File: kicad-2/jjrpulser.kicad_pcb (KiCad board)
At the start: 2 copper layers, 33.8 x 48 mm, 24 parts, among them J1 Conn_Coaxial_Power, J3 Screw_Terminal_HOT, J4 Screw_Terminal_COLD, J5 Conn_UART, U1 ESP-12, U2 AMS1117-3.3_SOT223

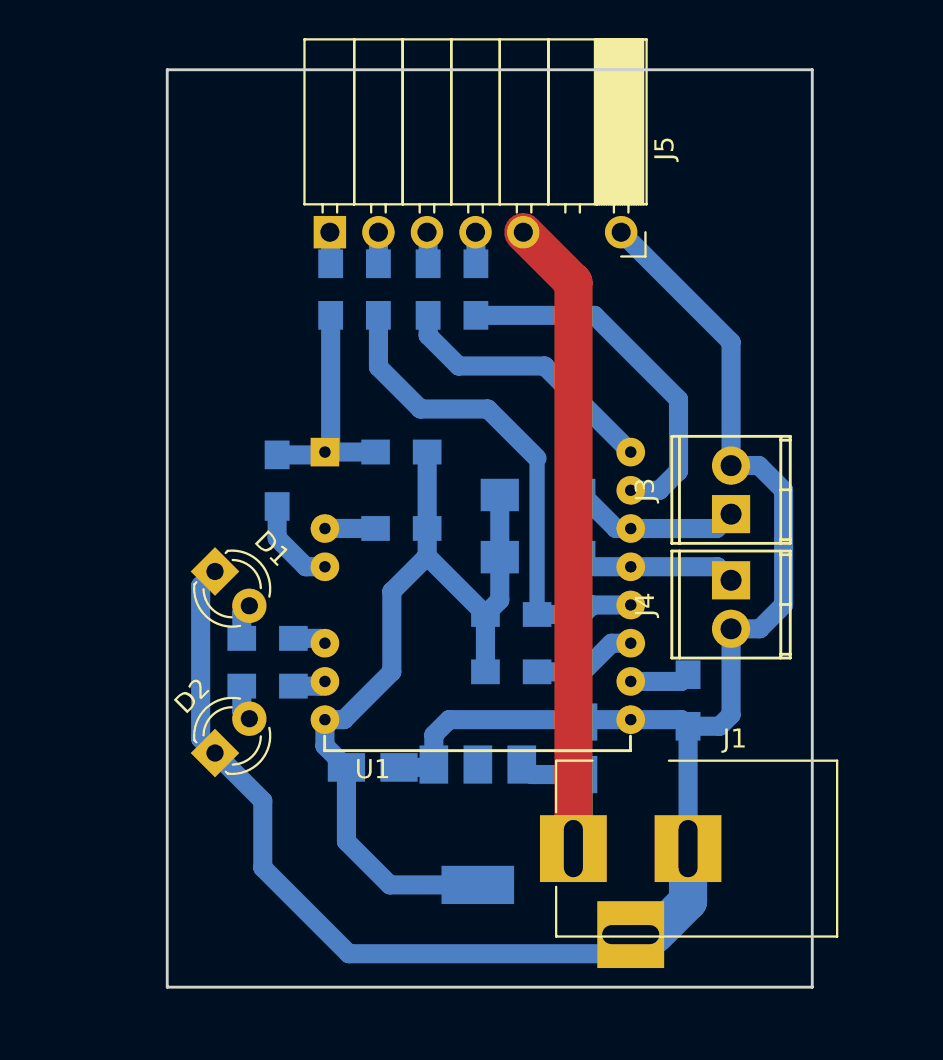
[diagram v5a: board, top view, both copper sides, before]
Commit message: Разводка2: Защитные резисторы на подключении водосчетчиков
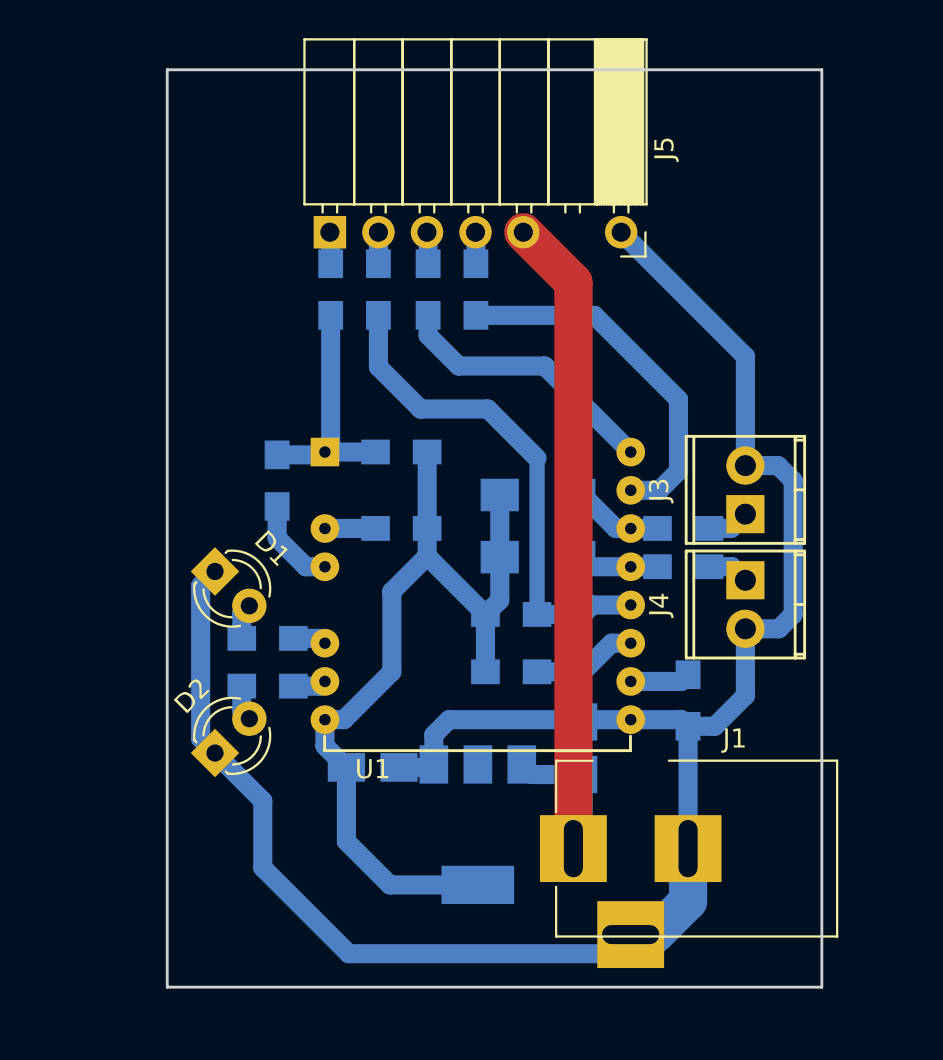
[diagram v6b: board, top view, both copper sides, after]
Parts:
- added R15: 470, Resistors_SMD:R_0805_HandSoldering, B.Cu at (166.2, 109.0)
- added R16: 470, Resistors_SMD:R_0805_HandSoldering, B.Cu at (166.2, 111.0)
- moved J3 0.75 mm to (169.5, 108.2)
- moved J4 0.75 mm to (169.5, 114.2)
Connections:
- R10 pad 2: Net-(J4-Pad1) -> Net-(R10-Pad2)
- R5 pad 1: Net-(J3-Pad2) -> Net-(R15-Pad2)
- U1 pad 13: Net-(J4-Pad1) -> Net-(R10-Pad2)
- U1 pad 14: Net-(J3-Pad2) -> Net-(R15-Pad2)
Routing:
- net Net-(J3-Pad2): track 9.14 -> 2.21 mm
- net Net-(J4-Pad1): track 8.60 -> 2.19 mm
- net Net-(R15-Pad2): track 0.00 -> 4.98 mm
- net Net-(R10-Pad2): track 0.00 -> 4.46 mm
- net Earth: track 101.2 -> 101.7 mm
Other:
- board size 33.8 x 48 mm -> 34.2 x 48 mm

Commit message: Новые маленькие коннекторы для счетчиков и питания
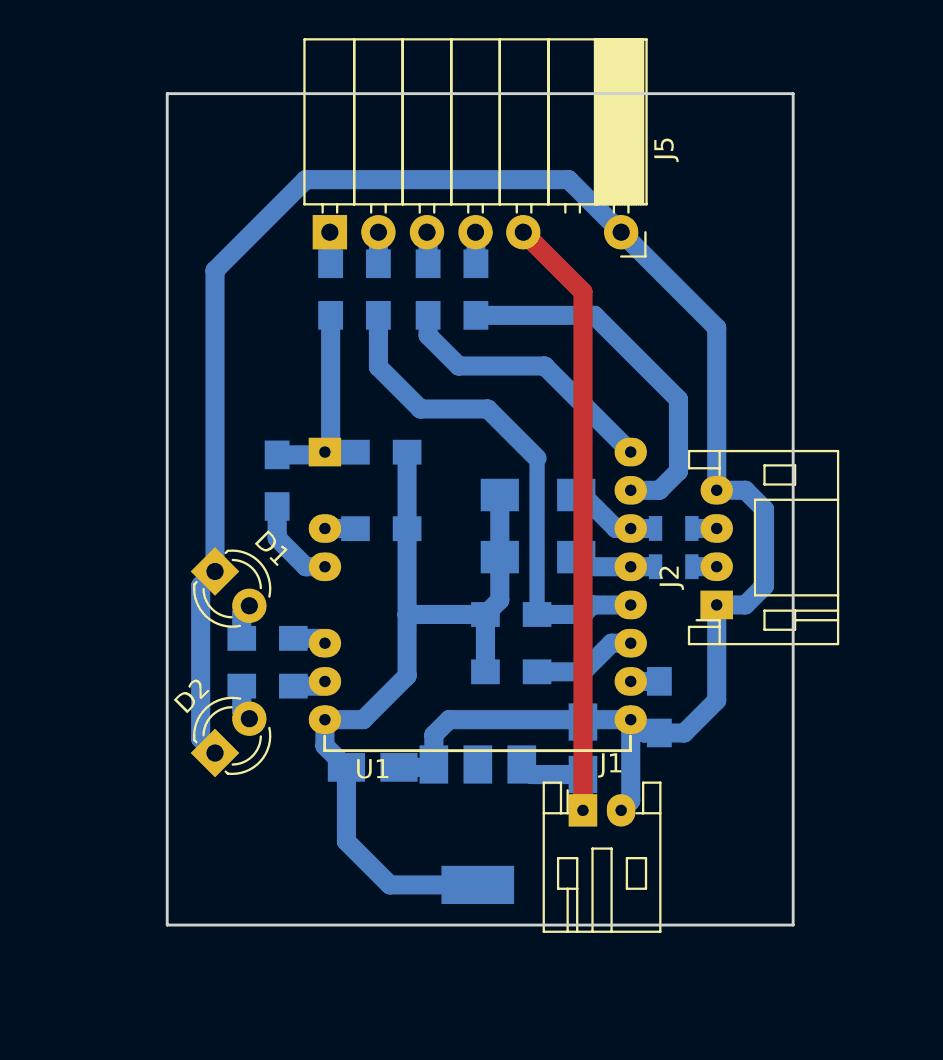
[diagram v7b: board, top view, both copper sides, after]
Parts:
- removed J3: Screw_Terminal_HOT, Connectors_Terminal_Blocks:TerminalBlock_Pheonix_MPT-2.54mm_2pol
- removed J4: Screw_Terminal_COLD, Connectors_Terminal_Blocks:TerminalBlock_Pheonix_MPT-2.54mm_2pol
- added J2: Hot&Cold Terminal, Connectors_JST:JST_PH_S4B-PH-K_04x2.00mm_Angled, F.Cu at (168.0, 113.0)
- J1: value Conn_Coaxial_Power -> 5V Input; footprint Connectors:BARREL_JACK -> Connectors_JST:JST_PH_S2B-PH-K_02x2.00mm_Angled
- R15, R16: footprint Resistors_SMD:R_0805_HandSoldering -> Resistors_SMD:R_0805
- moved J1 2.06 mm to (161.0, 123.8), turned to 0 degrees
- moved R6 1.54 mm to (165.0, 118.3)
- moved R2 1.05 mm to (150.4, 105.0)
- moved R3 1.05 mm to (150.4, 109.0)
- moved R15 0.50 mm to (165.8, 109.0)
- moved R16 0.50 mm to (165.8, 111.0)
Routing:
- net +5V: track 40.8 -> 36.8 mm
- net Earth: track 101.7 -> 105.3 mm
- net Net-(R6-Pad2): track 3.15 -> 1.50 mm
- net Net-(J2-Pad3): track 2.21 -> 1.00 mm
- net Net-(J2-Pad2): track 2.19 -> 1.00 mm
- net Net-(R3-Pad1): track 2.65 -> 1.61 mm
- net Net-(R11-Pad2): track 12.5 -> 11.4 mm
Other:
- board size 34.2 x 48 mm -> 32.8 x 43.5 mm

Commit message: Новая разводка. Котик и лисичка.
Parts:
- added Ref**: Val**, 1296354, F.Cu at (167.2, 90.5)
- added Ref**: Val**, cute_kittens_vector_set, F.Cu at (142.0, 89.5)
